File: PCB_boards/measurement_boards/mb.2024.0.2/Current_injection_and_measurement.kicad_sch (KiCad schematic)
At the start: 28 parts, among them J12 Conn_01x08_Socket, J14 Conn_01x02_Socket, J15 Conn_01x08_Socket, J20 shunt +, J21 shunt -, K3 G5LE-1, K4 G5LE-1, K5 G5LE-1, K6 G5LE-1, K7 G5LE-1, Q3 ZVN4206ASTZ, Q4 ZVN4206ASTZ, Q5 ZVN4206ASTZ, Q6 ZVN4206ASTZ, Q7 ZVN4206ASTZ, U5 1085

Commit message: update measurement board
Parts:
- removed D9: 1N4001, Diode_THT:D_DO-41_SOD81_P10.16mm_Horizontal, symbol Diode:1N4001
- removed K7: G5LE-1, Relay_THT:Relay_SPDT_Omron-G5LE-1, symbol Relay:G5LE-1
- removed Q7: ZVN4206ASTZ, Package_TO_SOT_THT:TO-92L_Wide, symbol ZVN4206ASTZ:ZVN4206ASTZ
- removed R8: 1k, Resistor_THT:R_Axial_DIN0207_L6.3mm_D2.5mm_P7.62mm_Horizontal, symbol Device:R
- removed R9: 100k, Resistor_THT:R_Axial_DIN0207_L6.3mm_D2.5mm_P7.62mm_Horizontal, symbol Device:R
- J12, J15: value Conn_01x08_Socket -> Conn_01x08_Female; symbol Connector:Conn_01x08_Socket -> Connector:Conn_01x08_Female
- J14: value Conn_01x02_Socket -> Conn_01x02_Female; symbol Connector:Conn_01x02_Socket -> Connector:Conn_01x02_Female
- Q3, Q4, Q5, Q6: symbol ZVN4206ASTZ:ZVN4206ASTZ -> ZVN4206A:ZVN4206ASTZ; Manufacturer_Name Diodes Incorporated -> Diodes Inc.
- renumbered D4 to D10, D7 to D11, D8 to D12, D3 to D9
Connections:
- net Input_DPS_+_alim renamed Input_DSP_+_alim
- net Input_DPS_GND_alim renamed Input_DSP_GND_alim
- no-connect marks 20 -> 19
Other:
- moved on the sheet: U5

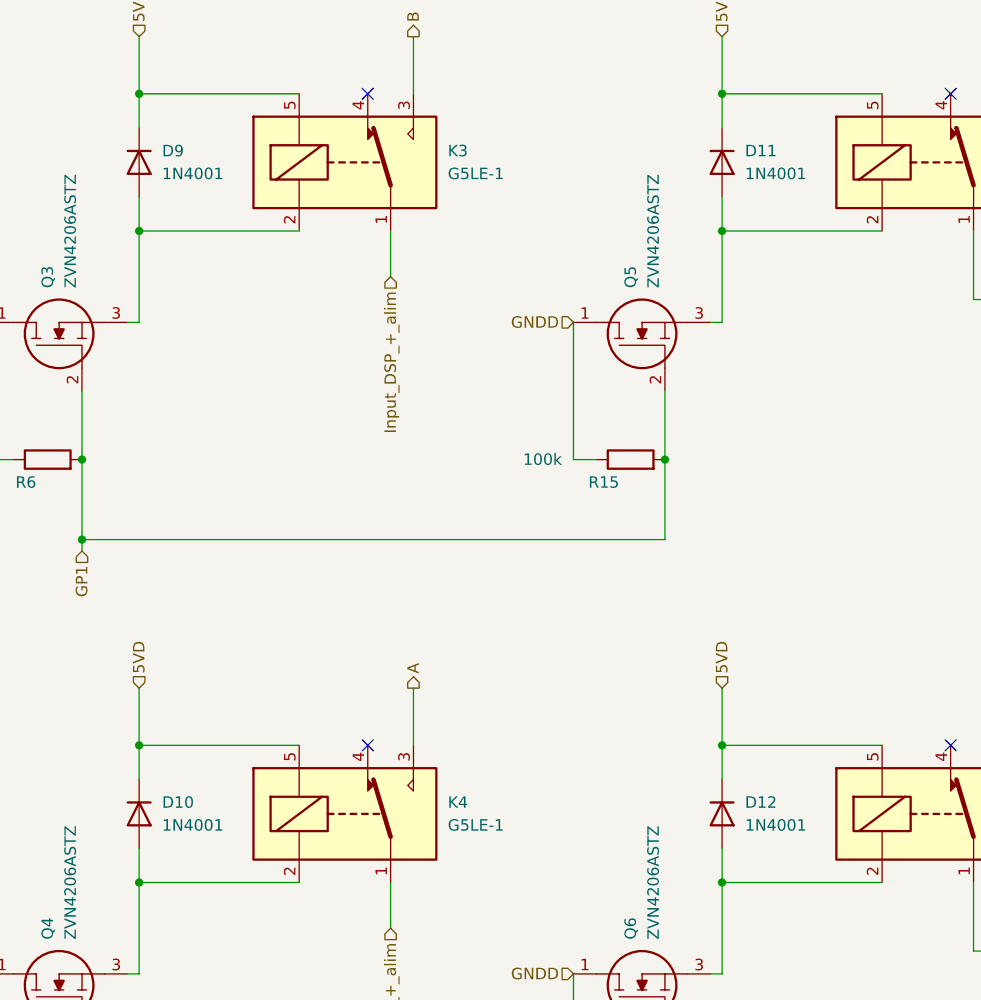
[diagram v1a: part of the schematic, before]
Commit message: update diode 1n4007
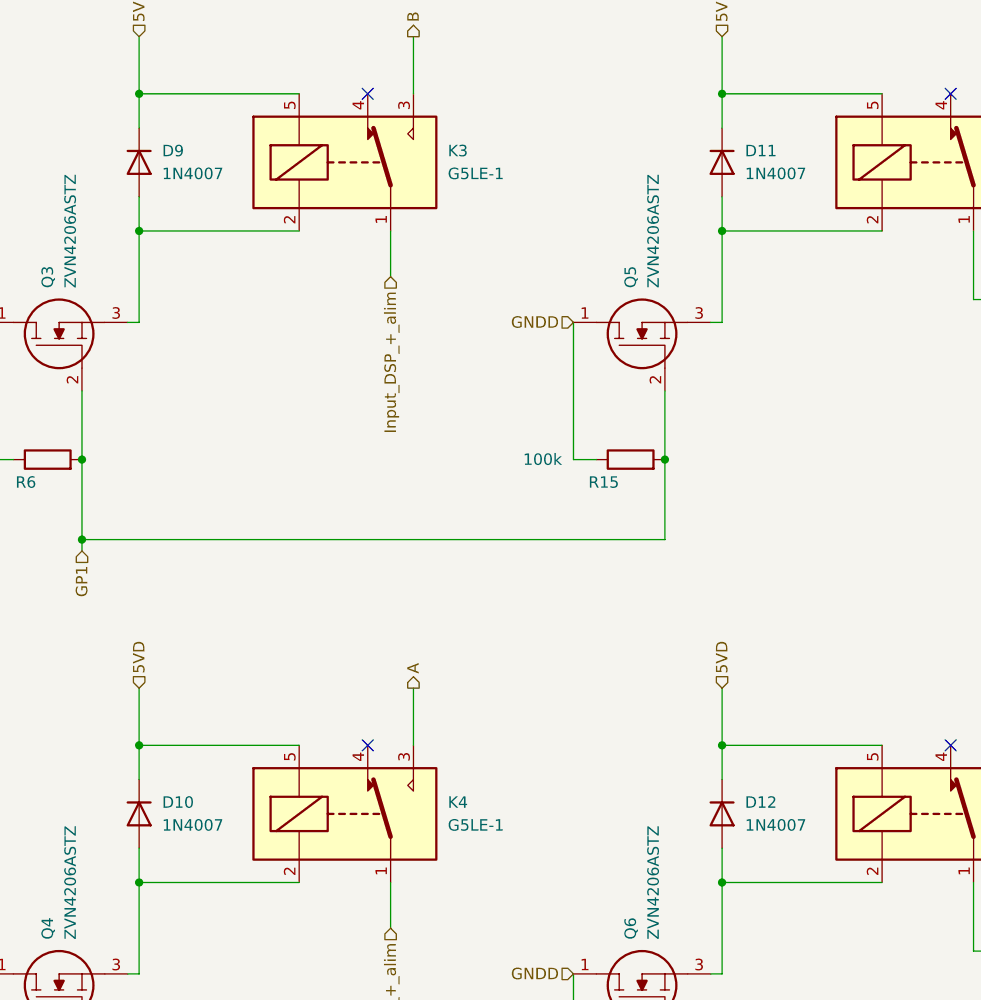
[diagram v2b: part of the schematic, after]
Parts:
- D10, D11, D12, D9: value 1N4001 -> 1N4007
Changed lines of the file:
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@@
       (effects (font (size 1.27 1.27)) (justify left))
     )
-    (property "Value" "1N4001" (at 49.53 36.8299 90)
+    (property "Value" "1N4007" (at 49.53 36.8299 90)
       (effects (font (size 1.27 1.27)) (justify left))
     )
@@
       (effects (font (size 1.27 1.27)) (justify left))
     )
-    (property "Value" "1N4001" (at 114.3 109.2199 90)
+    (property "Value" "1N4007" (at 114.3 109.2199 90)
       (effects (font (size 1.27 1.27)) (justify left))
     )
@@
       (effects (font (size 1.27 1.27)) (justify left))
     )
-    (property "Value" "1N4001" (at 49.53 109.2199 90)
+    (property "Value" "1N4007" (at 49.53 109.2199 90)
       (effects (font (size 1.27 1.27)) (justify left))
     )
@@
       (effects (font (size 1.27 1.27)) (justify left))
     )
-    (property "Value" "1N4001" (at 114.3 36.8299 90)
-      (effects (font (size 1.27 1.27)) (justify left))
-    )
+    (property "Value" "1N4007" (at 114.3 36.8299 90)
+      (effects (font (size 1.27 1.27)) (justify left))
+    )
